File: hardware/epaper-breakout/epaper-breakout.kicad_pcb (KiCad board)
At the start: 4 copper layers, 100 x 45 mm, 109 parts, among them J1 XF2M-3315-1A, J2 C10418, J3 Conn_02x05_Counter_Clockwise, J4 ED060SC4, J5 Conn_01x02_Female, J7 Conn_01x12, Q3 MMBT3904, Q4 MMBT3904, U1 MCP1700-3302E_SOT23, U11 TP4056, U12 CH340C, U2 PCA9535PW, U3 TPS651851RSLR, U4 XC6206PxxxMR, U5 ESP32-WROVER, U6 ED060XC5, U7 TPS2113APW

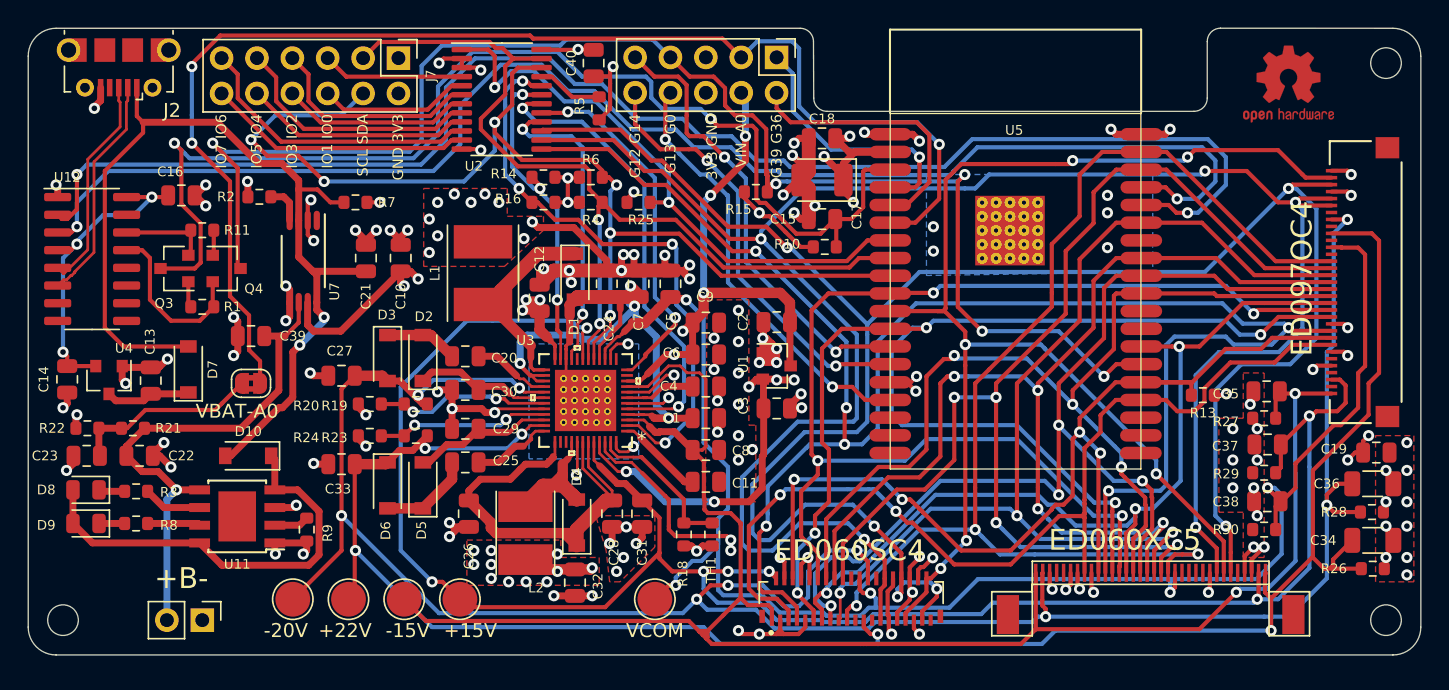
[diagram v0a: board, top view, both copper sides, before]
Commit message: Modified version adding 13.3 connector #4
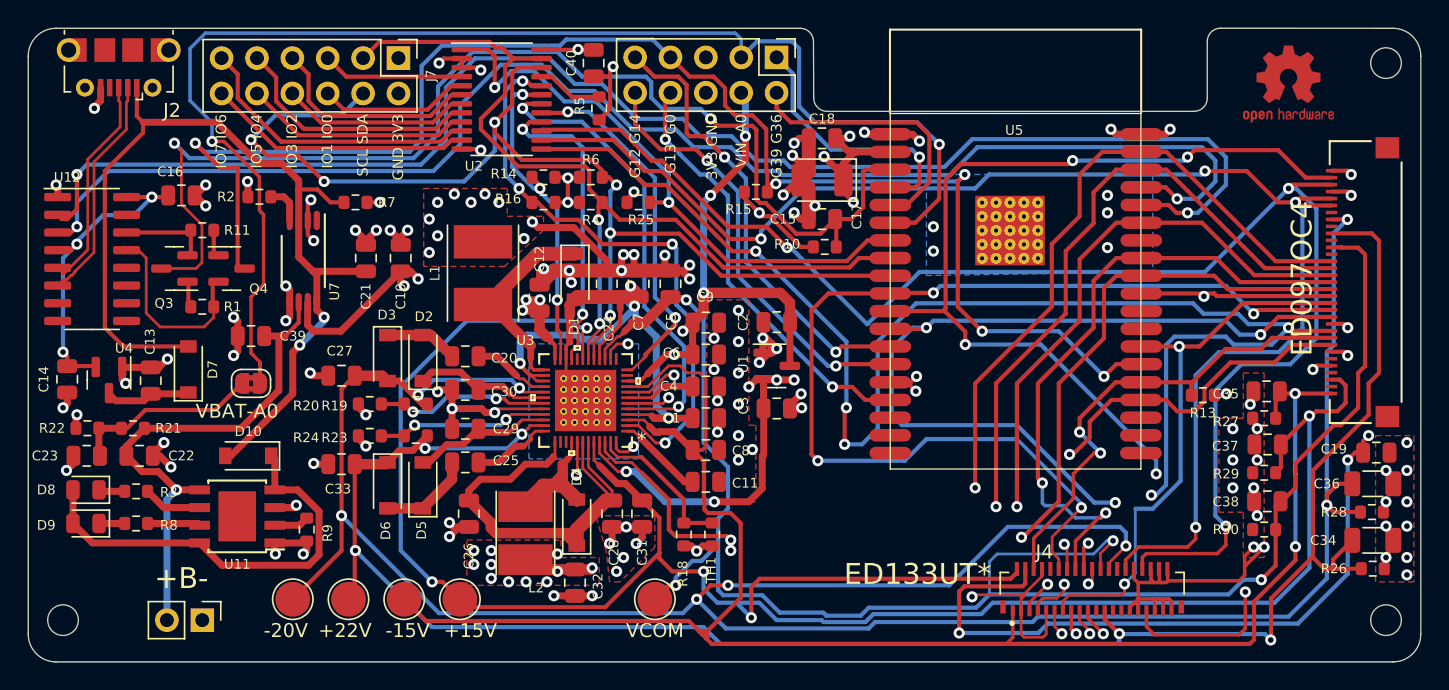
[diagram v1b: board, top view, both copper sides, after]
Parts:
- removed U6: ED060XC5, epaper-breakout:X05A20H34G
- C15, C16, C21, C22, C23, C39, C40: value 0.1uF -> 100nF
- J4: value ED060SC4 -> ED133UT2
- TH1: value 10k -> 10k/3380K
- U3: value TPS651851RSLR -> RSL48_4P4X4P4
- U7: value TPS2113APW -> Val**
- moved J4 17.3 mm to (101.4, 59.9)
- moved Q4 0.35 mm to (39.6, 36.8)
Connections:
- net /~DTR renamed /~{DTR}
- net /~GPIO_INTR renamed /~{GPIO_INTR}
- net /~RTS renamed /~{RTS}
- J1 pad 2: Net-(J1-Pad2) -> unconnected-(J1-Pad2)
- J1 pad 21: Net-(J1-Pad21) -> unconnected-(J1-Pad21)
- J1 pad 23: Net-(J1-Pad23) -> unconnected-(J1-Pad23)
- J1 pad 25: Net-(J1-Pad25) -> unconnected-(J1-Pad25)
- J1 pad 27: Net-(J1-Pad27) -> unconnected-(J1-Pad27)
- J1 pad 34: Net-(J1-Pad34) -> unconnected-(J1-Pad34)
- J1 pad 35: Net-(J1-Pad35) -> unconnected-(J1-Pad35)
- J1 pad 4: Net-(J1-Pad4) -> unconnected-(J1-Pad4)
- J1 pad 6: Net-(J1-Pad6) -> unconnected-(J1-Pad6)
- J2 pad 4: Net-(J2-Pad4) -> unconnected-(J2-Pad4)
- J4 pad 10: EPD_VDD -> unconnected-(J4-Pad10)
- J4 pad 20: Net-(J4-Pad20) -> GND
- J4 pad 21: Net-(J4-Pad21) -> unconnected-(J4-Pad21)
- J4 pad 25: Net-(J4-Pad25) -> unconnected-(J4-Pad25)
- J4 pad 26: Net-(J4-Pad26) -> unconnected-(J4-Pad26)
- J4 pad 27: /EP_MODE -> unconnected-(J4-Pad27)
- J4 pad 29: EPD_VDD -> GND
- J4 pad 30: EPD_VDD -> GND
- J4 pad 35: EPD_VDD -> GND
- J4 pad 36: EPD_VDD -> GND
- J4 pad 37: /EP_STV -> GND
- J4 pad 38: /EP_CKV -> GND
- J4 pad 39: Net-(J4-Pad39) -> GND
- J4 pad 8: EPD_VDD -> GND
- U11 pad 9: Net-(U11-Pad9) -> unconnected-(U11-Pad9)
- U12 pad 10: Net-(U12-Pad10) -> unconnected-(U12-Pad10)
- U12 pad 11: Net-(U12-Pad11) -> unconnected-(U12-Pad11)
- U12 pad 12: Net-(U12-Pad12) -> unconnected-(U12-Pad12)
- U12 pad 15: Net-(U12-Pad15) -> unconnected-(U12-Pad15)
- U12 pad 7: Net-(U12-Pad7) -> unconnected-(U12-Pad7)
- U12 pad 8: Net-(U12-Pad8) -> unconnected-(U12-Pad8)
- U12 pad 9: Net-(U12-Pad9) -> unconnected-(U12-Pad9)
- U3 pad 11: Net-(U3-Pad11) -> unconnected-(U3-Pad11)
- U3 pad 13: Net-(U3-Pad13) -> unconnected-(U3-Pad13)
- U3 pad 20: Net-(U3-Pad20) -> unconnected-(U3-Pad20)
- U3 pad 38: Net-(U3-Pad38) -> unconnected-(U3-Pad38)
- U3 pad 39: Net-(U3-Pad39) -> unconnected-(U3-Pad39)
- U5 pad 17: Net-(U5-Pad17) -> unconnected-(U5-Pad17)
- U5 pad 18: Net-(U5-Pad18) -> unconnected-(U5-Pad18)
- U5 pad 19: Net-(U5-Pad19) -> unconnected-(U5-Pad19)
- U5 pad 20: Net-(U5-Pad20) -> unconnected-(U5-Pad20)
- U5 pad 21: Net-(U5-Pad21) -> unconnected-(U5-Pad21)
- U5 pad 22: Net-(U5-Pad22) -> unconnected-(U5-Pad22)
- U5 pad 27: Net-(U5-Pad27) -> unconnected-(U5-Pad27)
- U5 pad 28: Net-(U5-Pad28) -> unconnected-(U5-Pad28)
- U5 pad 32: Net-(U5-Pad32) -> unconnected-(U5-Pad32)
- U7 pad 1: Net-(U7-Pad1) -> unconnected-(U7-Pad1)
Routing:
- net GND: track 295.2 -> 250.6 mm, vias 135 -> 128
- net /EP_MODE: track 146.2 -> 102.1 mm, vias 5 -> 4
- net /EP_STV: track 144.7 -> 106.0 mm, vias 6 -> 3
- net /EP_LE: track 72.4 -> 35.0 mm, vias 4 -> 2
- net EPD_VDD: track 38.9 -> 72.1 mm, vias 13 -> 8
- net /EP_D4: track 76.7 -> 46.4 mm, vias 4 -> 2
- net /EP_D6: track 86.1 -> 56.3 mm, vias 4 -> 2
- net /EP_D1: track 63.4 -> 40.4 mm, vias 3 -> 2
- net /EP_D3: track 73.3 -> 51.2 mm, vias 4 -> 2
- net /EP_CKH: track 69.7 -> 48.4 mm
- net /EP_D5: track 74.2 -> 56.7 mm, vias 3 -> 2
- net /15V: track 144.4 -> 160.0 mm, vias 7 -> 5
- net /EP_D7: track 83.4 -> 67.9 mm, vias 3 -> 2
- net /-20V: track 164.7 -> 179.8 mm, vias 9 -> 8
- net /EP_D2: track 70.8 -> 57.3 mm, vias 3 -> 2
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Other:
- board size 100 x 45 mm -> 100 x 45.5 mm
- net class Default removed
- board text added: "ED133UT*"
- board text removed: "ED060SC4"
- board text removed: "ED060XC5"

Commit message: #4 Fix some DRC warnings
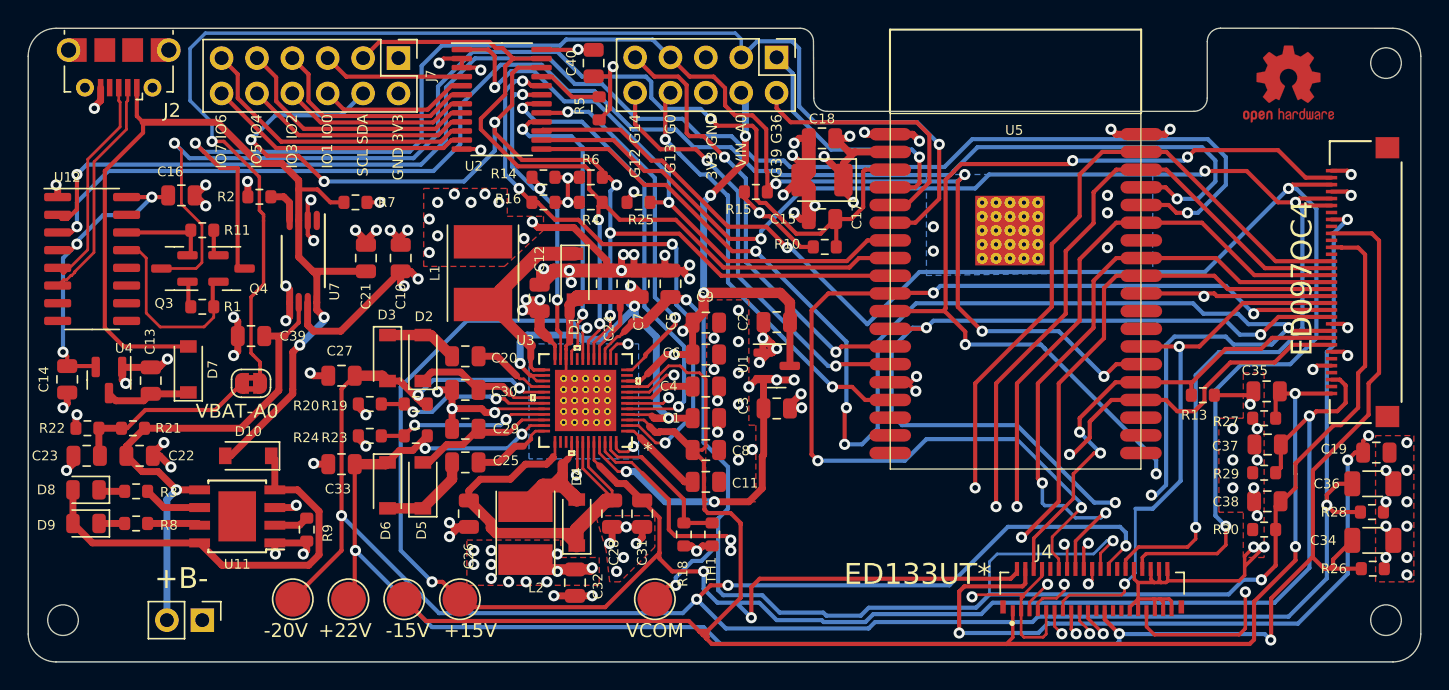
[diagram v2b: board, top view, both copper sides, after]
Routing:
- net GND: track 250.6 -> 252.6 mm, vias 128 -> 127
- net /EP_D3: track 51.2 -> 50.3 mm
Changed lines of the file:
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@@
     (property "Sheetname" "")
     (attr smd)
-    (fp_text reference "R13" (at 0 1.27) (layer "F.SilkS")
+    (fp_text reference "R13" (at -0.622 1.428) (layer "F.SilkS")
       (effects (font (size 0.7 0.7) (thickness 0.12)))
     )
@@
     (property "Sheetname" "")
     (attr smd)
-    (fp_text reference "C35" (at 2.928 -0.18) (layer "F.SilkS")
+    (fp_text reference "C35" (at 0.853 1.495) (layer "F.SilkS")
       (effects (font (size 0.7 0.7) (thickness 0.12)))
     )
@@
       (effects (font (size 1 1) (thickness 0.15)))
     )
-    (fp_text user "*" (at -4.035001 -2.781 180) (layer "F.SilkS")
+    (fp_text user "*" (at -4.476 -3.547 180) (layer "F.SilkS")
       (effects (font (size 1 1) (thickness 0.15)))
     )
-    (fp_text user "*" (at -4.035001 -2.781 180) (layer "F.SilkS")
+    (fp_text user "*" (at -4.035001 -2.781 180) (layer "F.SilkS") hide
       (effects (font (size 1 1) (thickness 0.15)))
     )
@@
   (segment (start 106.7 59.3) (end 106.825 59.175) (width 0.25) (layer "F.Cu") (net 1))
   (segment (start 72.0812 56.6716) (end 72.6316 56.6716) (width 0.5) (layer "F.Cu") (net 1))
-  (segment (start 110.172 45.847) (end 110.943 45.847) (width 0.3) (layer "F.Cu") (net 1))
   (segment (start 77.8 40.6) (end 77.8 41.7) (width 0.5) (layer "F.Cu") (net 1))
+  (segment (start 110.172 45.847) (end 112.701 45.847) (width 0.3) (layer "F.Cu") (net 1))
   (segment (start 67.604 36.896) (end 67.604 35.896) (width 0.5) (layer "F.Cu") (net 1))
   (segment (start 58.763181 46.827999) (end 58.496777 47.094403) (width 0.2) (layer "F.Cu") (net 1))
@@
   (segment (start 77.75 42.793) (end 78.457 42.793) (width 0.5) (layer "F.Cu") (net 1))
   (segment (start 48.705 48.955) (end 49.25 49.5) (width 0.5) (layer "F.Cu") (net 1))
-  (segment (start 110.943 45.847) (end 111.04 45.75) (width 0.3) (layer "F.Cu") (net 1))
   (segment (start 117.522602 43.727398) (end 117.25 44) (width 0.3) (layer "F.Cu") (net 1))
   (segment (start 106.7 59.3) (end 106.35 59.3) (width 0.25) (layer "F.Cu") (net 1))
@@
   (segment (start 33.8 43.85) (end 34.4 43.85) (width 0.5) (layer "F.Cu") (net 1))
   (segment (start 45.074998 32.042912) (end 45.300758 31.817152) (width 0.3) (layer "F.Cu") (net 1))
+  (segment (start 112.701 45.847) (end 112.978 45.57) (width 0.3) (layer "F.Cu") (net 1))
   (segment (start 70.576992 46.438008) (end 70.993 46.022) (width 0.2) (layer "F.Cu") (net 1))
   (segment (start 62.738 36.896) (end 63.854 36.896) (width 1) (layer "F.Cu") (net 1))
@@
   (via (at 76 48.75) (size 0.8) (drill 0.4) (layers "F.Cu" "B.Cu") (net 1))
   (via (at 37.75 32.25) (size 0.8) (drill 0.4) (layers "F.Cu" "B.Cu") (net 1))
-  (via (at 111.04 45.75) (size 0.8) (drill 0.4) (layers "F.Cu" "B.Cu") (net 1))
   (via (at 102.5 31.5) (size 0.8) (drill 0.4) (layers "F.Cu" "B.Cu") (net 1))
   (via (at 68.451743 49.531257) (size 0.8) (drill 0.4) (layers "F.Cu" "B.Cu") (net 1))
@@
   (via (at 96.325 56.05) (size 0.8) (drill 0.4) (layers "F.Cu" "B.Cu") (net 15))
   (via (at 100.25 62.975) (size 0.8) (drill 0.4) (layers "F.Cu" "B.Cu") (net 15))
-  (segment (start 101.4 61.825) (end 101.4 60.7) (width 0.2) (layer "In2.Cu") (net 15))
-  (segment (start 100.35 56.3) (end 99.9 55.85) (width 0.2) (layer "In2.Cu") (net 15))
-  (segment (start 99.9 55.85) (end 96.525 55.85) (width 0.2) (layer "In2.Cu") (net 15))
-  (segment (start 96.525 55.85) (end 96.325 56.05) (width 0.2) (layer "In2.Cu") (net 15))
-  (segment (start 101.4 60.7) (end 100.35 59.65) (width 0.2) (layer "In2.Cu") (net 15))
-  (segment (start 100.25 62.975) (end 101.4 61.825) (width 0.2) (layer "In2.Cu") (net 15))
-  (segment (start 100.35 59.65) (end 100.35 56.3) (width 0.2) (layer "In2.Cu") (net 15))
+  (segment (start 96.525 55.85) (end 99.9 55.85) (width 0.2) (layer "In2.Cu") (net 15))
+  (segment (start 100.35 56.3) (end 100.35 62.875) (width 0.2) (layer "In2.Cu") (net 15))
+  (segment (start 100.35 62.875) (end 100.25 62.975) (width 0.2) (layer "In2.Cu") (net 15))
+  (segment (start 96.325 56.05) (end 96.525 55.85) (width 0.2) (layer "In2.Cu") (net 15))
+  (segment (start 99.9 55.85) (end 100.35 56.3) (width 0.2) (layer "In2.Cu") (net 15))
   (segment (start 104.93 36) (end 103.13 36) (width 0.3) (layer "F.Cu") (net 16))
   (segment (start 97.5 51.825) (end 97.825 52.15) (width 0.3) (layer "F.Cu") (net 16))
@@
   (segment (start 38.25 37.7) (end 38.25 39.425) (width 0.3) (layer "F.Cu") (net 38))
   (segment (start 34.475 40.95) (end 37.625 40.95) (width 0.2) (layer "F.Cu") (net 38))
-  (segment (start 38.325 35.725) (end 38.25 35.8) (width 0.3) (layer "F.Cu") (net 39))
   (segment (start 38.325 34) (end 38.325 35.725) (width 0.3) (layer "F.Cu") (net 39))
   (segment (start 32.05 50.2) (end 32.05 49.52) (width 0.5) (layer "F.Cu") (net 40))
